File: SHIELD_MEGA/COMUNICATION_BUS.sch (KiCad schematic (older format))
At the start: 4 parts, among them J12 Conn_01x04_Male, J13 Conn_01x04_Male, J14 Conn_01x06_Male, J15 Conn_01x04_Male

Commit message: Changing symbol on comunication sheet
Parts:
- removed J14: Conn_01x06_Male, Connector_PinHeader_2.54mm:PinHeader_1x06_P2.54mm_Vertical, symbol Connector:Conn_01x06_Male
- added J14, J3: Conn_02x03_Odd_Even, Connector_PinSocket_2.54mm:PinSocket_2x03_P2.54mm_Vertical, symbol Connector_Generic:Conn_02x03_Odd_Even
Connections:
- wire segments 18 -> 24
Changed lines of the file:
@@
 Text HLabel 7900 3850 2    50   Input ~ 0
 DGND
-Wire Wire Line
-	5950 5450 5750 5450
-Text HLabel 5950 5350 2    50   Input ~ 0
+Text HLabel 6250 4450 2    50   Input ~ 0
 5V
-Text HLabel 5950 5450 2    50   Input ~ 0
+Text HLabel 6250 4650 2    50   Input ~ 0
 DGND
 Wire Wire Line
@@
 Wire Wire Line
 	7700 3550 7900 3550
-Wire Wire Line
-	5750 5250 5950 5250
-Text HLabel 5950 5250 2    50   Input ~ 0
+Text HLabel 5350 4650 0    50   Input ~ 0
 SPI_RST
-Text HLabel 5950 5150 2    50   Input ~ 0
+Text HLabel 5350 4550 0    50   Input ~ 0
 SCK
-Wire Wire Line
-	5950 5150 5750 5150
-Wire Wire Line
-	5750 5050 5950 5050
-Text HLabel 5950 5050 2    50   Input ~ 0
+Text HLabel 6250 4550 2    50   Input ~ 0
 MOSI
-Text HLabel 5950 4950 2    50   Input ~ 0
+Text HLabel 5350 4450 0    50   Input ~ 0
 MISO
-Wire Wire Line
-	5950 4950 5750 4950
 $Comp
 L Connector:Conn_01x04_Male J12
@@
 $EndComp
 $Comp
-L Connector:Conn_01x06_Male J14
-U 1 1 61C38C33
-P 5550 5150
-F 0 "J14" H 5658 5531 50  0000 C CNN
-F 1 "Conn_01x06_Male" H 5658 5440 50  0000 C CNN
-F 2 "Connector_PinHeader_2.54mm:PinHeader_1x06_P2.54mm_Vertical" H 5550 5150 50  0001 C CNN
-F 3 "~" H 5550 5150 50  0001 C CNN
-	1    5550 5150
-	1    0    0    -1
+L Connector_Generic:Conn_02x03_Odd_Even J14
+U 1 1 619D2485
+P 5850 4550
+F 0 "J14" H 5900 4867 50  0000 C CNN
+F 1 "Conn_02x03_Odd_Even" H 5900 4776 50  0000 C CNN
+F 2 "Connector_PinSocket_2.54mm:PinSocket_2x03_P2.54mm_Vertical" H 5850 4550 50  0001 C CNN
+F 3 "~" H 5850 4550 50  0001 C CNN
+	1    5850 4550
+	-1   0    0    -1
 $EndComp
 Wire Wire Line
-	5750 5350 5950 5350
+	6250 4550 6050 4550
+Wire Wire Line
+	6250 4450 6050 4450
+Wire Wire Line
+	6250 4650 6050 4650
+Wire Wire Line
+	5350 4450 5550 4450
+Wire Wire Line
+	5550 4550 5350 4550
+Wire Wire Line
+	5350 4650 5550 4650
+Text HLabel 6250 5100 2    50   Input ~ 0
+5V
+Text HLabel 6250 5300 2    50   Input ~ 0
+DGND
+Text HLabel 5350 5300 0    50   Input ~ 0
+SPI_RST
+Text HLabel 5350 5200 0    50   Input ~ 0
+SCK
+Text HLabel 6250 5200 2    50   Input ~ 0
+MOSI
+Text HLabel 5350 5100 0    50   Input ~ 0
+MISO
+$Comp
+L Connector_Generic:Conn_02x03_Odd_Even J3
+U 1 1 61AF3820
+P 5850 5200
+F 0 "J3" H 5900 5517 50  0000 C CNN
+F 1 "Conn_02x03_Odd_Even" H 5900 5426 50  0000 C CNN
+F 2 "Connector_PinSocket_2.54mm:PinSocket_2x03_P2.54mm_Vertical" H 5850 5200 50  0001 C CNN
+F 3 "~" H 5850 5200 50  0001 C CNN
+	1    5850 5200
+	-1   0    0    -1
+$EndComp
+Wire Wire Line
+	6250 5200 6050 5200
+Wire Wire Line
+	6250 5100 6050 5100
+Wire Wire Line
+	6250 5300 6050 5300
+Wire Wire Line
+	5350 5100 5550 5100
+Wire Wire Line
+	5550 5200 5350 5200
+Wire Wire Line
+	5350 5300 5550 5300
 $EndSCHEMATC

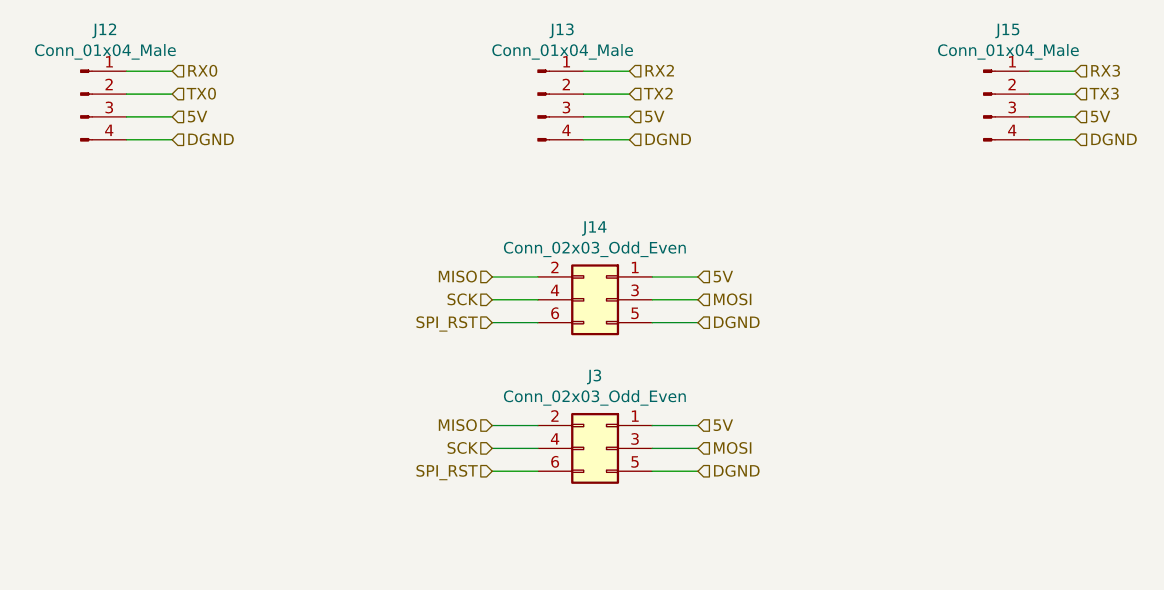
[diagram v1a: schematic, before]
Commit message: Removind redudant ICSP interface
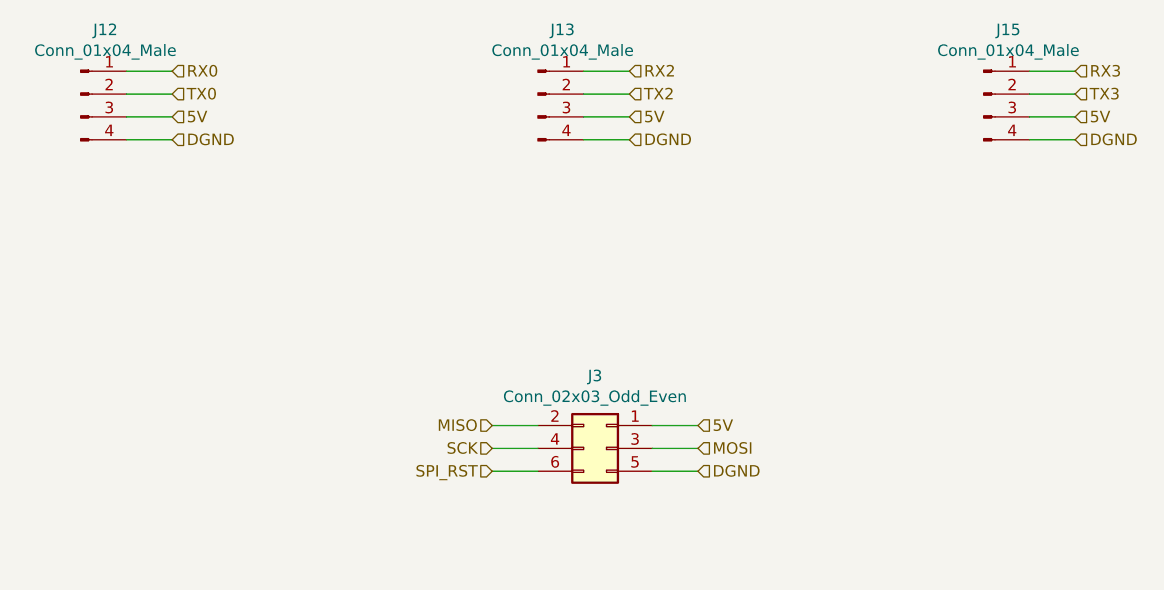
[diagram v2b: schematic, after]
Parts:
- removed J14: Conn_02x03_Odd_Even, Connector_PinSocket_2.54mm:PinSocket_2x03_P2.54mm_Vertical, symbol Connector_Generic:Conn_02x03_Odd_Even
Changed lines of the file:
@@
 Text HLabel 7900 3850 2    50   Input ~ 0
-DGND
-Text HLabel 6250 4450 2    50   Input ~ 0
-5V
-Text HLabel 6250 4650 2    50   Input ~ 0
 DGND
 Wire Wire Line
@@
 Wire Wire Line
 	7700 3550 7900 3550
-Text HLabel 5350 4650 0    50   Input ~ 0
-SPI_RST
-Text HLabel 5350 4550 0    50   Input ~ 0
-SCK
-Text HLabel 6250 4550 2    50   Input ~ 0
-MOSI
-Text HLabel 5350 4450 0    50   Input ~ 0
-MISO
 $Comp
 L Connector:Conn_01x04_Male J12
@@
 	1    0    0    -1
 $EndComp
-$Comp
-L Connector_Generic:Conn_02x03_Odd_Even J14
-U 1 1 619D2485
-P 5850 4550
-F 0 "J14" H 5900 4867 50  0000 C CNN
-F 1 "Conn_02x03_Odd_Even" H 5900 4776 50  0000 C CNN
-F 2 "Connector_PinSocket_2.54mm:PinSocket_2x03_P2.54mm_Vertical" H 5850 4550 50  0001 C CNN
-F 3 "~" H 5850 4550 50  0001 C CNN
-	1    5850 4550
-	-1   0    0    -1
-$EndComp
-Wire Wire Line
-	6250 4550 6050 4550
-Wire Wire Line
-	6250 4450 6050 4450
-Wire Wire Line
-	6250 4650 6050 4650
-Wire Wire Line
-	5350 4450 5550 4450
-Wire Wire Line
-	5550 4550 5350 4550
-Wire Wire Line
-	5350 4650 5550 4650
 Text HLabel 6250 5100 2    50   Input ~ 0
 5V
